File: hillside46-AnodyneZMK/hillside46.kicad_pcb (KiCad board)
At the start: 2 copper layers, 142.5 x 99.9 mm, 92 parts, among them J1 Haptic, J2 TRRS, J3 Bat_Pos, J4 Bat_Neg, J5 Bat_Pos, J6 Bat_Neg, K1 SW_Key, K10 SW_Key, K11 SW_Key, K12 SW_Key, K13 SW_Key, K14 SW_Key, K15 SW_Key, K16 SW_Key, K17 SW_Key, K18 SW_Key, K19 SW_Rotary, K2 SW_Key, K20 SW_Rotary, K21 SW_Key, K22 SW_Key, K23 SW_Key, K3 SW_Key, K4 SW_Key, K5 SW_Key, K6 SW_Key, K7 SW_Key, K8 SW_Key, K9 SW_Key, SW1 SKQGAFE010, SW2 SW_Power, U1 ProMicro_r, U2 SRV05-4

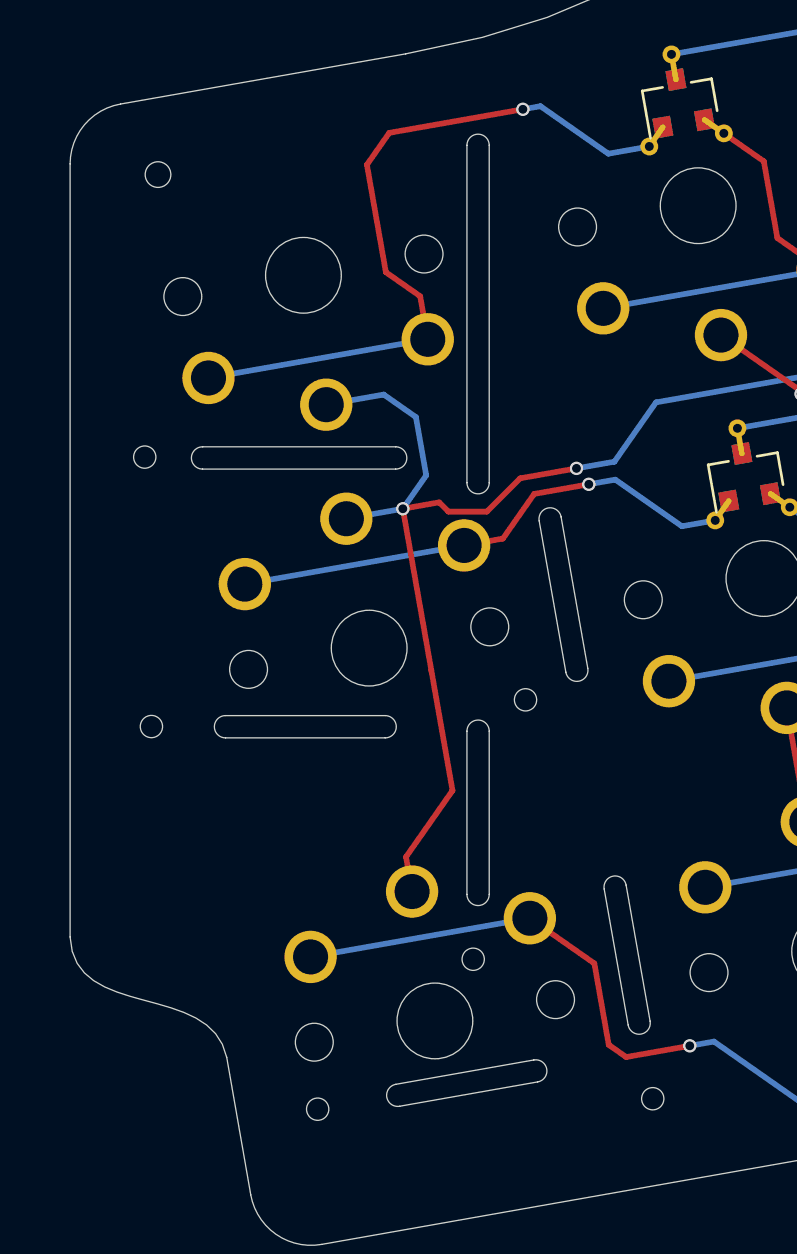
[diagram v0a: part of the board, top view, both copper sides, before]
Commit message: remove pinkie column cutouts
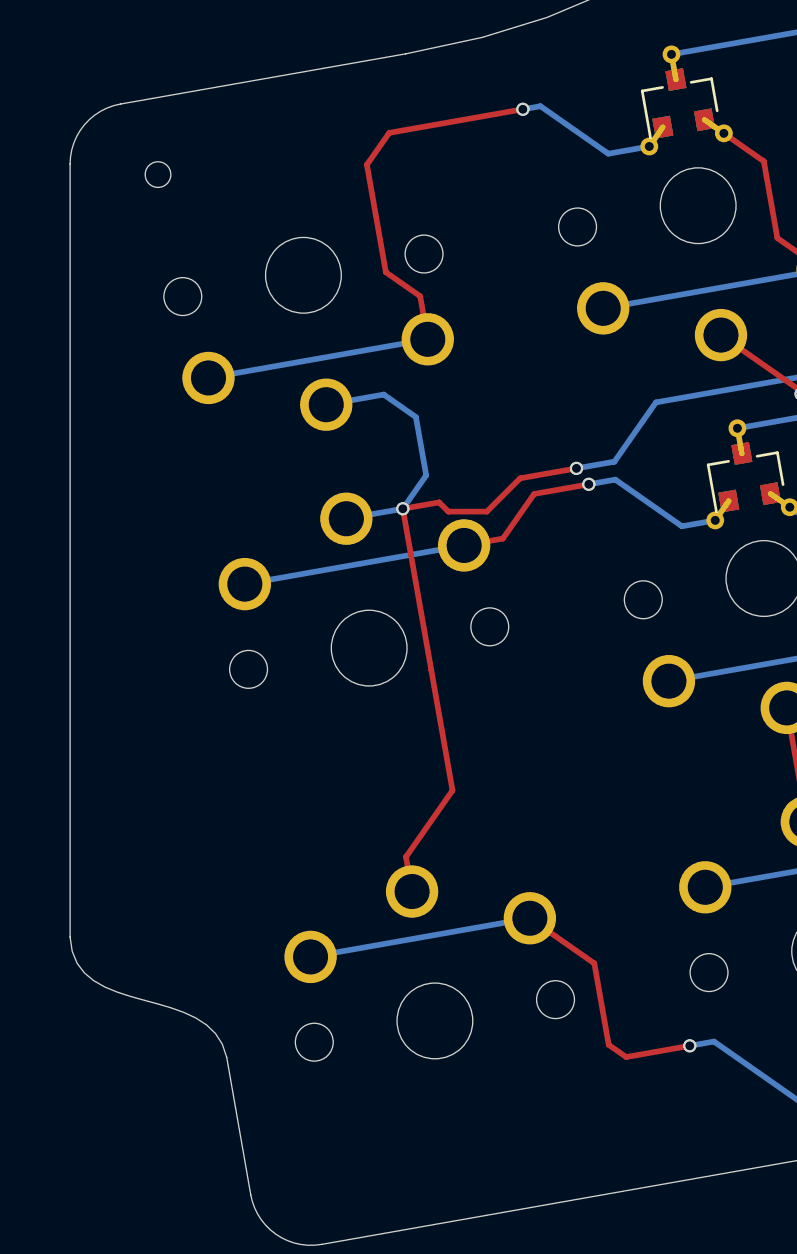
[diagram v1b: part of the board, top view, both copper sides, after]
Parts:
- removed H26, H27, H28, H29, H30, H31: Breakoff Hole, hillside_basic:HoleBreakoff_1mm
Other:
- outline, holes or cut-outs redrawn
- board text removed: "-2-"
- board text removed: "-br-"
- board text removed: "-cut 1-"
- board text removed: "-cut 2-"
- board text removed: "-cut 3-"
- board text removed: "-cut A-"
- board text removed: "-cut Z-"
- board text removed: "CUT"
- board text removed: "cut Y-"

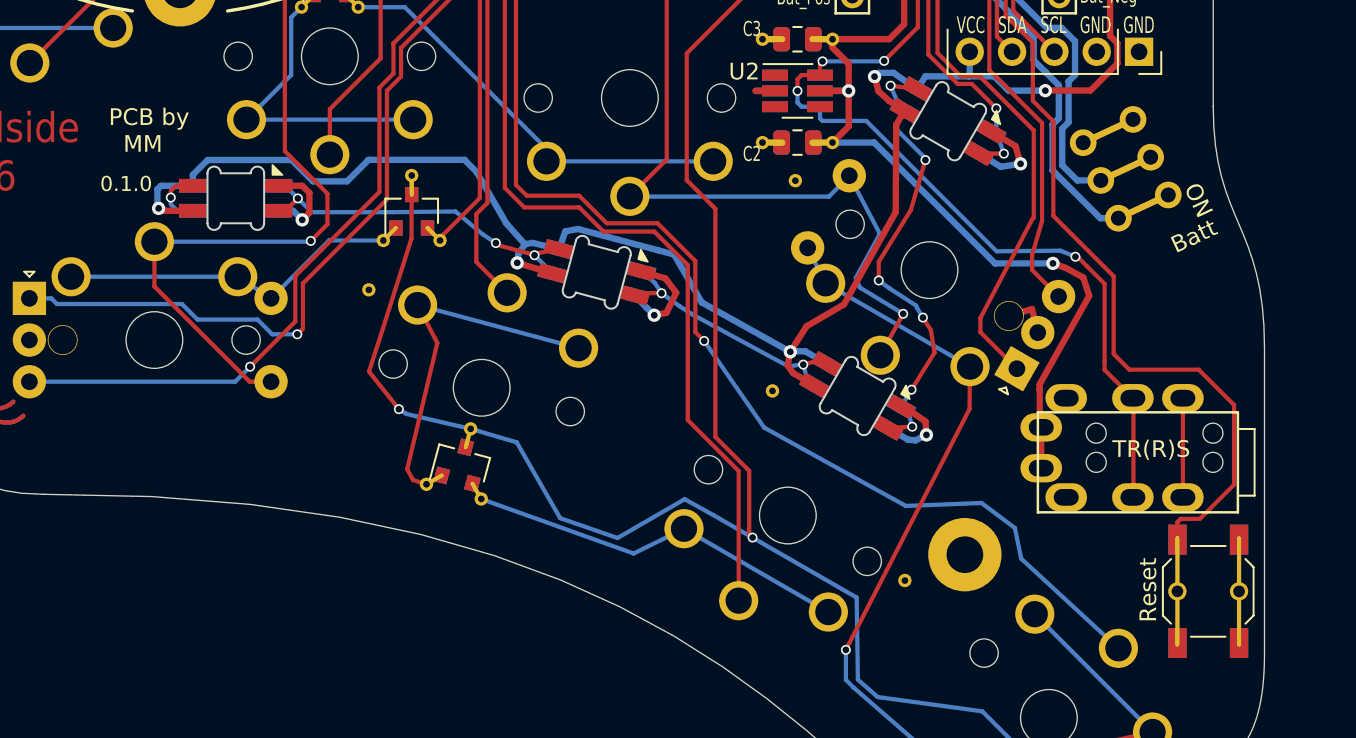
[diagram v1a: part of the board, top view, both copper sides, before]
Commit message: clean up silkscreen
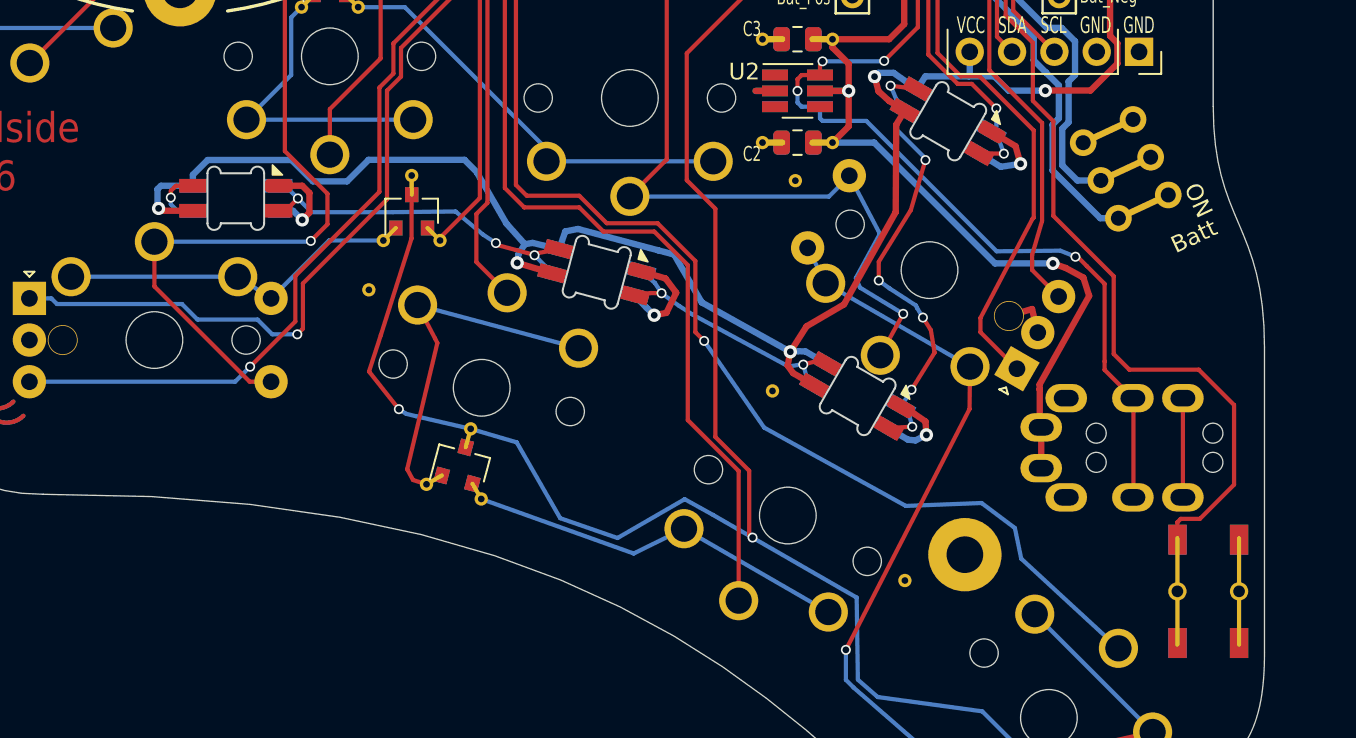
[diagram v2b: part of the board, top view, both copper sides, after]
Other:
- board text removed: "0.1.0"
- board text removed: "PCB by MM"
